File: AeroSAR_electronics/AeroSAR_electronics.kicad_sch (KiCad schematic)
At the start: 15 parts, among them J1 USB_B_Micro, J10 Receiver, J11 Rpi, J12 GPS, J2 ESC-1, J3 ESC-2, J4 Servo, J5 Servo, J6 Servo, J7 Servo, J8 Servo, J9 Compass

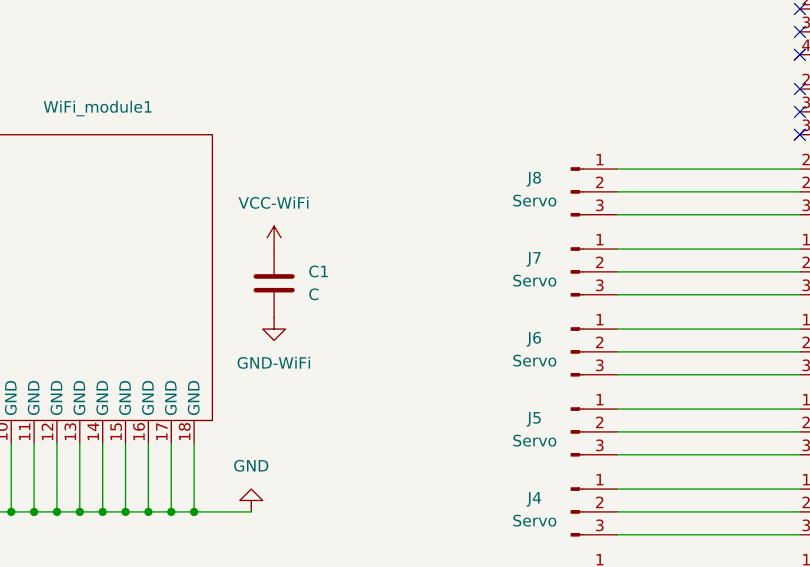
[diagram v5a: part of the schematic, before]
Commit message: Configured the FC footprint for mounting
Also added another capacitor and moved them closer to the WiFi module
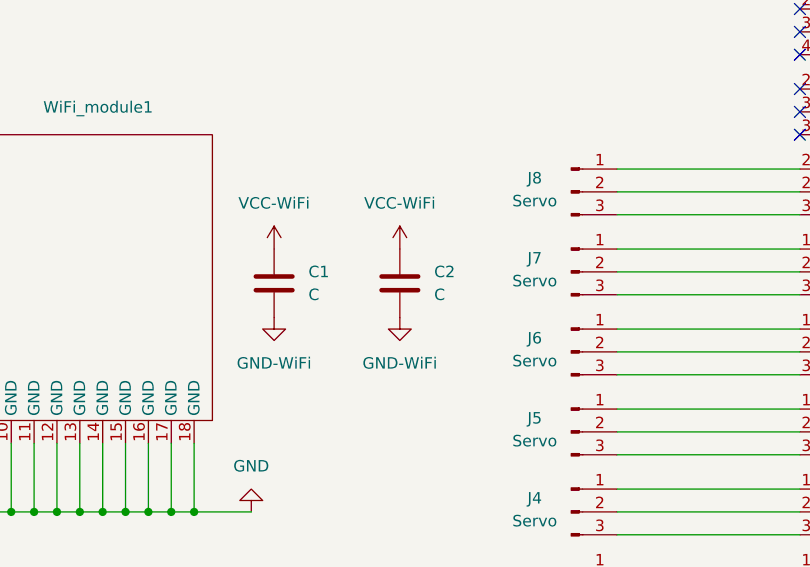
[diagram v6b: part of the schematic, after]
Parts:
- added C2: C, Capacitor_SMD:C_0805_2012Metric, symbol Device:C
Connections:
- net GND-WiFi: now also C2.2
- net VCC-WiFi: now also C2.1
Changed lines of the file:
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@@
+	)
+	(symbol
+		(lib_id "Device:C")
+		(at 140.97 72.39 0)
+		(unit 1)
+		(exclude_from_sim no)
+		(in_bom yes)
+		(on_board yes)
+		(dnp no)
+		(fields_autoplaced yes)
+		(property "Reference" "C2"
+			(at 144.78 71.1199 0)
+			(effects
+				(font
+					(size 1.27 1.27)
+				)
+				(justify left)
+			)
+		)
+		(property "Value" "C"
+			(at 144.78 73.6599 0)
+			(effects
+				(font
+					(size 1.27 1.27)
+				)
+				(justify left)
+			)
+		)
+		(property "Footprint" "Capacitor_SMD:C_0805_2012Metric"
+			(at 141.9352 76.2 0)
+			(effects
+				(font
+					(size 1.27 1.27)
+				)
+				(hide yes)
+			)
+		)
+		(property "Datasheet" "https://lcsc.com/datasheet/lcsc_datasheet_2504251652_AIDE-CAPACITOR-0805X5R106K500NT_C48579582.pdf"
+			(at 140.97 72.39 0)
+			(effects
+				(font
+					(size 1.27 1.27)
+				)
+				(hide yes)
+			)
+		)
+		(property "Description" "Unpolarized capacitor"
+			(at 140.97 72.39 0)
+			(effects
+				(font
+					(size 1.27 1.27)
+				)
+				(hide yes)
+			)
+		)
+		(property "LCSC" "C48579582"
+			(at 140.97 72.39 0)
+			(effects
+				(font
+					(size 1.27 1.27)
+				)
+				(hide yes)
+			)
+		)
+		(property "URL" "https://lcsc.com/product-detail/Multilayer-Ceramic-Capacitors-MLCC-SMD-SMT_AIDE-CAPACITOR-0805X5R106K500NT_C48579582.html?s_z=n_ceramic%2520capacitor%2520smd"
+			(at 140.97 72.39 0)
+			(effects
+				(font
+					(size 1.27 1.27)
+				)
+				(hide yes)
+			)
+		)
+		(pin "2"
+		)
+		(pin "1"
+		)
+		(instances
+			(project "AeroSAR_electronics"
+				(path "/da961784-12b1-4f58-8e7d-3aa55c43f0e3"
+					(reference "C2")
+					(unit 1)
+				)
+			)
+		)
 	)
 	(symbol
@@
 	)
 	(symbol
+		(lib_id "power:GND")
+		(at 140.97 76.2 0)
+		(unit 1)
+		(exclude_from_sim no)
+		(in_bom yes)
+		(on_board yes)
+		(dnp no)
+		(fields_autoplaced yes)
+		(property "Reference" "#PWR014"
+			(at 140.97 82.55 0)
+			(effects
+				(font
+					(size 1.27 1.27)
+				)
+				(hide yes)
+			)
+		)
+		(property "Value" "GND-WiFi"
+			(at 140.97 81.28 0)
+			(effects
+				(font
+					(size 1.27 1.27)
+				)
+			)
+		)
+		(property "Footprint" ""
+			(at 140.97 76.2 0)
+			(effects
+				(font
+					(size 1.27 1.27)
+				)
+				(hide yes)
+			)
+		)
+		(property "Datasheet" ""
+			(at 140.97 76.2 0)
+			(effects
+				(font
+					(size 1.27 1.27)
+				)
+				(hide yes)
+			)
+		)
+		(property "Description" "Power symbol creates a global label with name \"GND\" , ground"
+			(at 140.97 76.2 0)
+			(effects
+				(font
+					(size 1.27 1.27)
+				)
+				(hide yes)
+			)
+		)
+		(pin "1"
+		)
+		(instances
+			(project "AeroSAR_electronics"
+				(path "/da961784-12b1-4f58-8e7d-3aa55c43f0e3"
+					(reference "#PWR014")
+					(unit 1)
+				)
+			)
+		)
+	)
+	(symbol
 		(lib_id "power:VCC")
 		(at 255.27 74.93 270)
@@
 					(unit 1)
 				)
+			)
+		)
+	)
+	(symbol
+		(lib_id "power:VCC")
+		(at 140.97 68.58 0)
+		(unit 1)
+		(exclude_from_sim no)
+		(in_bom yes)
+		(on_board yes)
+		(dnp no)
+		(fields_autoplaced yes)
+		(property "Reference" "#PWR013"
+			(at 140.97 72.39 0)
+			(effects
+				(font
+					(size 1.27 1.27)
+				)
+				(hide yes)
+			)
+		)
+		(property "Value" "VCC-WiFi"
+			(at 140.97 63.5 0)
+			(effects
+				(font
+					(size 1.27 1.27)
+				)
+			)
+		)
+		(property "Footprint" ""
+			(at 140.97 68.58 0)
+			(effects
+				(font
+					(size 1.27 1.27)
+				)
+				(hide yes)
+			)
+		)
+		(property "Datasheet" ""
+			(at 140.97 68.58 0)
+			(effects
+				(font
+					(size 1.27 1.27)
+				)
+				(hide yes)
+			)
+		)
+		(property "Description" "Power symbol creates a global label with name \"VCC\""
+			(at 140.97 68.58 0)
+			(effects
+				(font
+					(size 1.27 1.27)
+				)
+				(hide yes)
+			)
+		)
+		(pin "1"
+		)
+		(instances
+			(project "AeroSAR_electronics"
+				(path "/da961784-12b1-4f58-8e7d-3aa55c43f0e3"
+					(reference "#PWR013")
+					(unit 1)
+				)
